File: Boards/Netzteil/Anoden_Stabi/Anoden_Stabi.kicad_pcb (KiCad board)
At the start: 2 copper layers, 100 x 80 mm, 26 parts, among them P1 CONN_4, P2 CONN_2, P3 CONN_2, P4 CONN_2, Q1 2SC2979, Q2 MJE5731

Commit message: Layouting...
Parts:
- removed R8: 30k, Resistors_ThroughHole:Resistor_Horizontal_RM10mm
- P2, P3, P4: footprint Sockets_Mini-Universal:MiniUniversalMate-N-LokSocket_2PinHorizontal -> MiniUniversalMate-N-LokSockets_13Aug2012:MiniUniversalMate-N-LokSocket_2PinVertical_12Aug2012
- moved C4 48.5 mm to (163.8, 60.3), turned to 270 degrees
- moved C7 41.9 mm to (129.5, 92.1), turned to 270 degrees
- moved R7 34.2 mm to (160.0, 78.7), turned to 0 degrees
- moved C8 24.8 mm to (145.4, 85.1)
- moved R3 23.6 mm to (124.5, 83.2), turned to 90 degrees
- moved P4 21.3 mm to (164.5, 101.0), turned to 0 degrees
- moved C5 18.4 mm to (145.4, 64.1), turned to 0 degrees
- moved R5 15.9 mm to (106.0, 53.3)
- moved R4 14.0 mm to (90.2, 101.0), turned to 0 degrees
- moved P2 9.32 mm to (164.5, 114.9), turned to 0 degrees
- moved Q2 6.87 mm to (102.9, 114.3), turned to 90 degrees
- moved P3 5.88 mm to (164.5, 88.3), turned to 0 degrees
- moved C2 5.85 mm to (111.1, 98.4), turned to 0 degrees
- moved C1 4.96 mm to (130.2, 74.3)
- moved R6 4.62 mm to (95.2, 97.2)
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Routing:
- net Net-(D1-Pad1): track 8.26 -> 39.0 mm
- net Net-(Q2-Pad2): track 6.06 -> 30.1 mm
- net -120V: track 80.4 -> 57.8 mm
- net +450V: track 48.4 -> 30.1 mm
- net +240V: track 54.7 -> 72.6 mm
- net +300V: track 97.9 -> 83.1 mm
- net Net-(C1-Pad1): track 38.9 -> 26.2 mm
- net Net-(C2-Pad1): track 32.0 -> 25.2 mm
- net Net-(D3-Pad1): track 16.6 -> 10.2 mm
- net -180V: track 22.3 -> 23.3 mm
- net Net-(Q1-Pad2): track 13.4 -> 14.0 mm

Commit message: Work in Progress
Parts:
- removed P4: CONN_2, MiniUniversalMate-N-LokSockets_13Aug2012:MiniUniversalMate-N-LokSocket_2PinVertical_12Aug2012
- P1: value CONN_4 -> CONN_3; footprint MiniUniversalMate-N-LokSockets_13Aug2012:MiniUniversalMate-N-LokSocket_4PinVertical_13Aug2012 -> Connectors_Mini-Universal:MiniUniversalMate-N-LokSocket_3PinVertical
- P2: footprint MiniUniversalMate-N-LokSockets_13Aug2012:MiniUniversalMate-N-LokSocket_2PinVertical_12Aug2012 -> Connectors_Mini-Universal:MiniUniversalMate-N-LokSocket_2PinVertical
- P3: value CONN_2 -> CONN_4; footprint MiniUniversalMate-N-LokSockets_13Aug2012:MiniUniversalMate-N-LokSocket_2PinVertical_12Aug2012 -> Connectors_Mini-Universal:MiniUniversalMate-N-LokSocket_4PinVertical
- moved R7 26.3 mm to (135.3, 87.6), turned to 90 degrees
- moved D2 25.4 mm to (118.7, 64.1), turned to 180 degrees
- moved R3 19.9 mm to (108.6, 71.1), turned to 0 degrees
- moved R5 15.3 mm to (121.0, 56.5)
- moved Q1 9.86 mm to (116.8, 80.6), turned to 90 degrees
- moved D1 9.61 mm to (108.6, 67.3), turned to 0 degrees
- moved R6 7.96 mm to (88.3, 93.3), turned to 0 degrees
- moved C4 7.62 mm to (163.8, 67.9), turned to 90 degrees
- moved C2 7.41 mm to (114.9, 104.8)
- moved P2 6.38 mm to (165.1, 108.6), turned to 270 degrees
- moved P1 5.43 mm to (84.5, 80.0), turned to 270 degrees
- moved C1 4.81 mm to (128.3, 69.8)
- moved C6 4.55 mm to (148.0, 109.9), turned to 0 degrees
- moved D3 4.49 mm to (88.3, 100.3), turned to 0 degrees
- moved R2 4.45 mm to (88.3, 97.2), turned to 0 degrees
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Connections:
- P1 pad 3: GND -> -180V
- P2 pad 1: -120V -> +450V
- P3 pad 2: GND -> +240V
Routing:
- net +450V: track 30.1 -> 131.7 mm, vias 0 -> 2
- net Net-(D1-Pad1): track 39.0 -> 8.25 mm
- net +240V: track 72.6 -> 45.7 mm
- net Net-(Q1-Pad2): track 14.0 -> 39.1 mm
- net +300V: track 83.1 -> 64.6 mm
- net -120V: track 57.8 -> 69.2 mm
- net Net-(Q2-Pad2): track 30.1 -> 40.9 mm
- net Net-(C1-Pad1): track 26.2 -> 19.8 mm
- net Net-(D3-Pad1): track 10.2 -> 6.98 mm
- net Net-(D1-Pad2): track 5.07 -> 3.17 mm
- net -180V: track 23.3 -> 22.6 mm

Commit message: Work in Progress
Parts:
- removed P3: CONN_4, Connectors_Mini-Universal:MiniUniversalMate-N-LokSocket_4PinVertical
- added J1: Conn_01x06, Connectors_Mini-Universal:MiniUniversalMate-N-LokSocket_6PinVertical, F.Cu at (166.4, 85.7)
- moved C4 23.3 mm to (141.0, 72.4)
- moved C5 14.0 mm to (159.4, 64.8)
- moved P1 5.85 mm to (88.3, 75.6)
- moved C1 3.45 mm to (127.0, 66.7), turned to 90 degrees
- moved P2 3.24 mm to (168.3, 109.2)
- moved R7 2.67 mm to (132.6, 87.6)
- moved R5 1.91 mm to (119.1, 56.5)
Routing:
- net +450V: track 131.7 -> 122.8 mm
- net -120V: track 69.2 -> 74.1 mm
- net Net-(C1-Pad1): track 19.8 -> 23.8 mm
- net +300V: track 64.6 -> 61.4 mm
- net Net-(C2-Pad1): track 25.4 -> 26.8 mm
- net Net-(Q1-Pad2): track 39.1 -> 38.3 mm
- net -180V: track 22.6 -> 23.1 mm
- net +240V: track 45.7 -> 45.2 mm
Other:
- board text added: "Bot"
- board text added: "D. Walter v1.0"

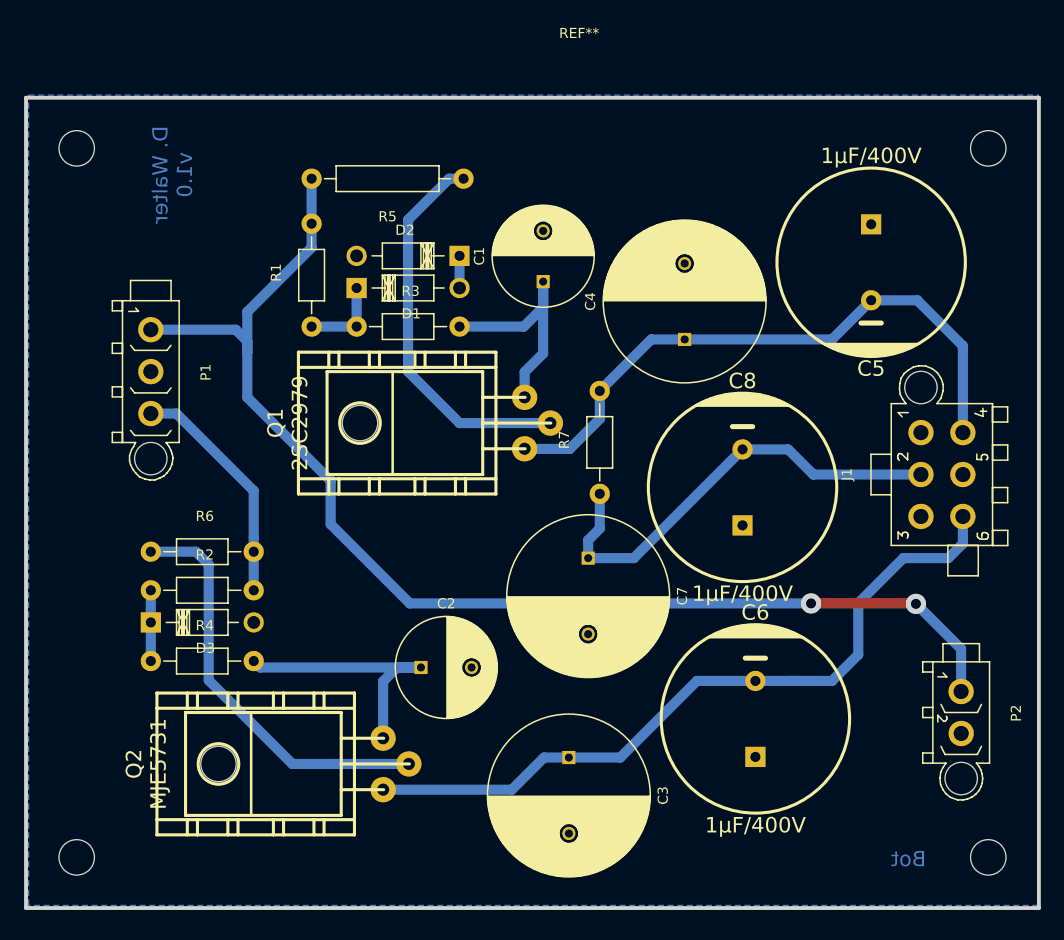
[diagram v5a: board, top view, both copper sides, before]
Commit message: Converted to Kicad 5.1 and Layout changes
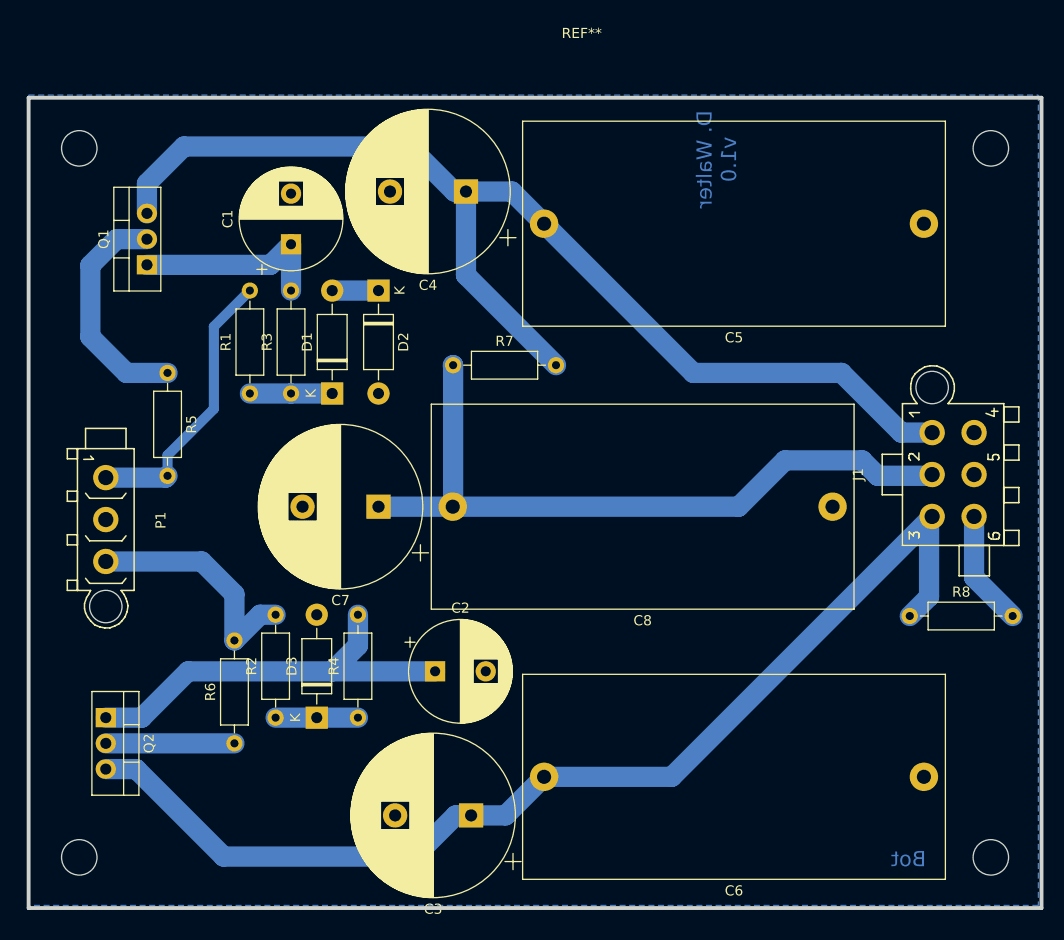
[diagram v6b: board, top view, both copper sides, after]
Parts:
- removed P2: CONN_2, Connectors_Mini-Universal:MiniUniversalMate-N-LokSocket_2PinVertical
- added R8: 10k, Resistor_THT:R_Axial_DIN0207_L6.3mm_D2.5mm_P10.16mm_Horizontal, F.Cu at (163.2, 99.7)
- C1, C2: footprint Capacitors_ThroughHole:C_Radial_D10_L16_P5 -> Capacitor_THT:CP_Radial_D10.0mm_P5.00mm
- C3, C4, C7: footprint Capacitors_ThroughHole:C_Radial_D16_L25_P7.5 -> Capacitor_THT:CP_Radial_D16.0mm_P7.50mm
- C5, C6, C8: footprint w_capacitors:CP_18x16mm -> Capacitor_THT:C_Rect_L41.5mm_W20.0mm_P37.50mm_MKS4
- D1, D2, D3: footprint Diodes_ThroughHole:Diode_DO-41_SOD81_Horizontal_RM10 -> Diode_THT:D_DO-41_SOD81_P10.16mm_Horizontal
- Q1, Q2: footprint w_to:to220-horiz_5772 -> Package_TO_SOT_THT:TO-220-3_Vertical
- R1, R2, R3, R4, R6, R7: footprint Resistors_ThroughHole:Resistor_Horizontal_RM10mm -> Resistor_THT:R_Axial_DIN0207_L6.3mm_D2.5mm_P10.16mm_Horizontal
- R5: footprint Resistors_ThroughHole:Resistor_Horizontal_RM15mm -> Resistor_THT:R_Axial_DIN0207_L6.3mm_D2.5mm_P10.16mm_Horizontal
- moved R5 35.0 mm to (89.9, 75.7), turned to 270 degrees
- moved Q1 32.9 mm to (87.9, 65.0)
- moved C4 26.1 mm to (119.4, 57.8), turned to 180 degrees
- moved C1 25.2 mm to (102.1, 63.0)
- moved C7 21.3 mm to (110.7, 88.9), turned to 180 degrees
- moved R4 21.2 mm to (108.7, 109.7), turned to 90 degrees
- moved R6 20.6 mm to (96.5, 112.3), turned to 90 degrees
- moved Q2 19.6 mm to (83.8, 109.7), turned to 270 degrees
- moved R7 19.3 mm to (118.1, 74.9), turned to 0 degrees
- moved D3 18.9 mm to (104.6, 109.7), turned to 90 degrees
- moved R2 17.6 mm to (100.6, 109.7), turned to 90 degrees
- moved C6 17.6 mm to (164.6, 115.6), turned to 180 degrees
- moved P1 15.3 mm to (83.8, 90.2)
- moved C3 11.2 mm to (119.9, 119.4), turned to 180 degrees
- moved D1 10.7 mm to (106.2, 77.7), turned to 90 degrees
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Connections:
- J1 pad 1: GND -> +300V
- J1 pad 3: GND -> -120V
- J1 pad 4: +300V -> GND
- J1 pad 6: -120V -> -60V
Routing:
- net +450V: track 122.8 -> 27.8 mm, vias 2 -> 0
- net +300V: track 61.4 -> 114.5 mm
- net -120V: track 74.1 -> 109.8 mm
- net Net-(Q2-Pad2): track 40.9 -> 12.7 mm
- net +240V: track 45.2 -> 71.3 mm
- net Net-(Q1-Pad2): track 38.3 -> 22.8 mm
- net Net-(C2-Pad1): track 26.8 -> 41.0 mm
- net -60V: track 0.00 -> 11.4 mm
- net Net-(C1-Pad1): track 23.8 -> 19.6 mm
- net Net-(D1-Pad2): track 3.17 -> 4.57 mm
- net Net-(D3-Pad1): track 6.98 -> 8.13 mm
- net -180V: track 23.1 -> 23.7 mm

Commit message: Layout changes, Supply connector changes, Mounting holes
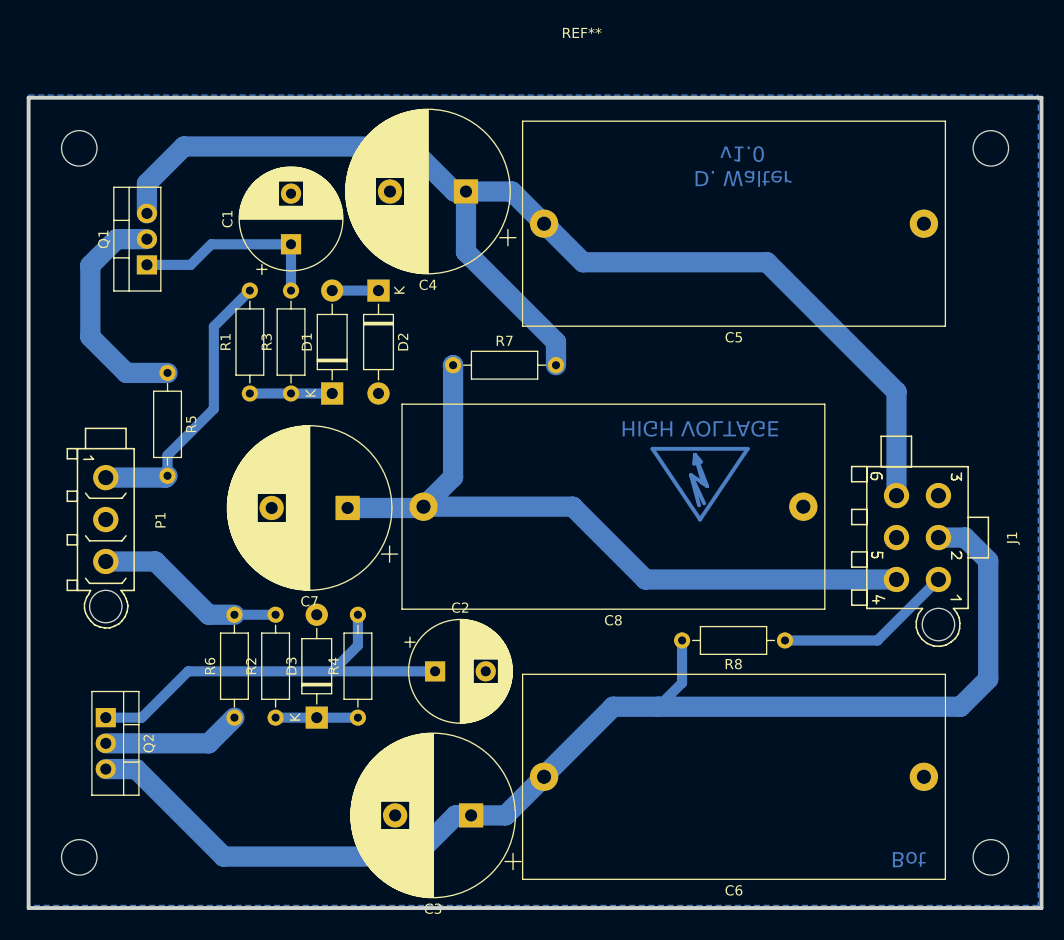
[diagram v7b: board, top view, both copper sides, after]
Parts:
- added REF**: Symbol_HighVoltage_Type2_CopperTop_VerySmall, Symbol:Symbol_HighVoltage_Type2_CopperTop_VerySmall, B.Cu at (142.5, 86.0)
- moved R8 12.6 mm to (150.9, 102.1), turned to 180 degrees
- moved J1 7.15 mm to (164.0, 91.9), turned to 270 degrees
- moved C7 3.05 mm to (107.7, 89.0)
- moved C8 2.89 mm to (152.7, 88.9)
- moved R6 2.54 mm to (96.5, 109.7)
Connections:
- J1 pad 1: +300V -> -60V
- J1 pad 2: +240V -> -120V
- J1 pad 3: -120V -> GND
- J1 pad 4: GND -> +240V
- J1 pad 6: -60V -> +300V
- R8 pad 1: -120V -> -60V
- R8 pad 2: -60V -> -120V
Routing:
- net -120V: track 109.8 -> 123.1 mm
- net -60V: track 11.4 -> 17.6 mm
- net +300V: track 114.5 -> 119.6 mm
- net -180V: track 23.7 -> 18.9 mm
- net +240V: track 71.3 -> 72.5 mm
- net Net-(Q2-Pad2): track 12.7 -> 13.8 mm
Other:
- board text added: "HIGH VOLTAGE"

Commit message: Added Vias & Mounting Holes
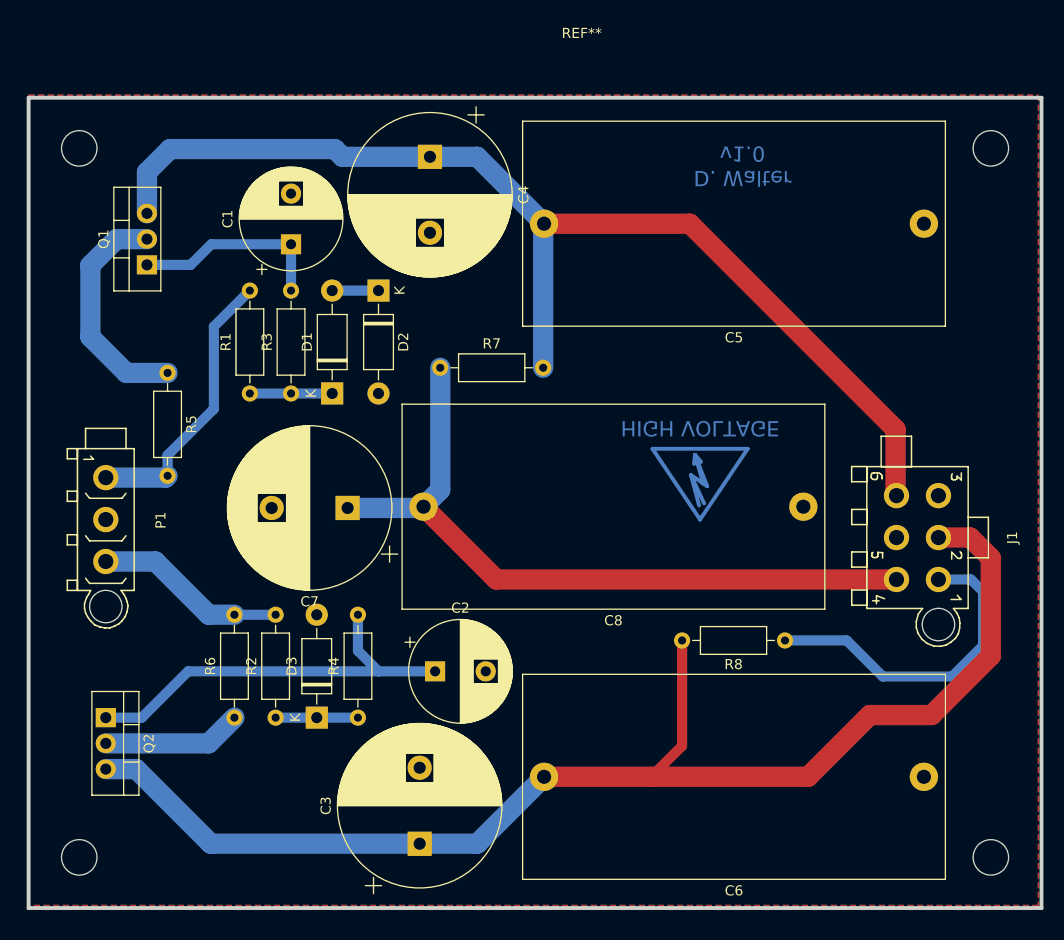
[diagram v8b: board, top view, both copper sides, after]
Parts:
- moved C3 5.80 mm to (114.8, 122.2), turned to 90 degrees
- moved C4 4.94 mm to (115.8, 54.4), turned to 270 degrees
- moved R7 1.30 mm to (116.8, 75.2)
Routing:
- net -60V: track 17.6 -> 32.5 mm
- net +300V: track 119.6 -> 111.3 mm
- net -120V: track 123.1 -> 128.6 mm
- net +240V: track 72.5 -> 71.6 mm
- added copper zone on F.Cu, net GND
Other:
- board text removed: "Bot"
